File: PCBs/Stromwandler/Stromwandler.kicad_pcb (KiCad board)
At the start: 2 copper layers, 30 x 30 mm, 10 parts, among them J1 Conn_02x05_Odd_Even, J4 2X, U1 HO15-NPxSP33

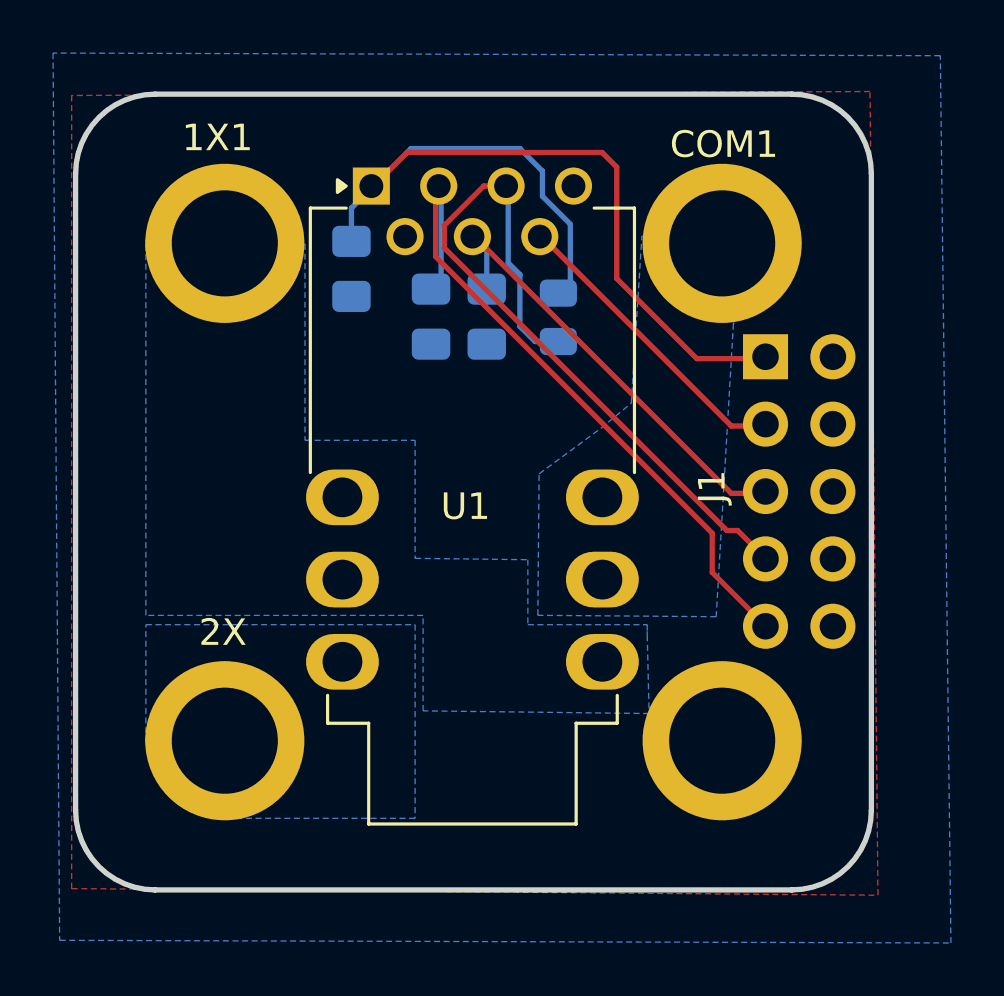
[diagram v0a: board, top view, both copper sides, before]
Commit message: Korrekturen: Anordnung 4mm-Pins Tausch Stecker Pin 5 7 (Uref, OCD) GND Vias (noch mehr  notwendig / Anordnung pruefen)
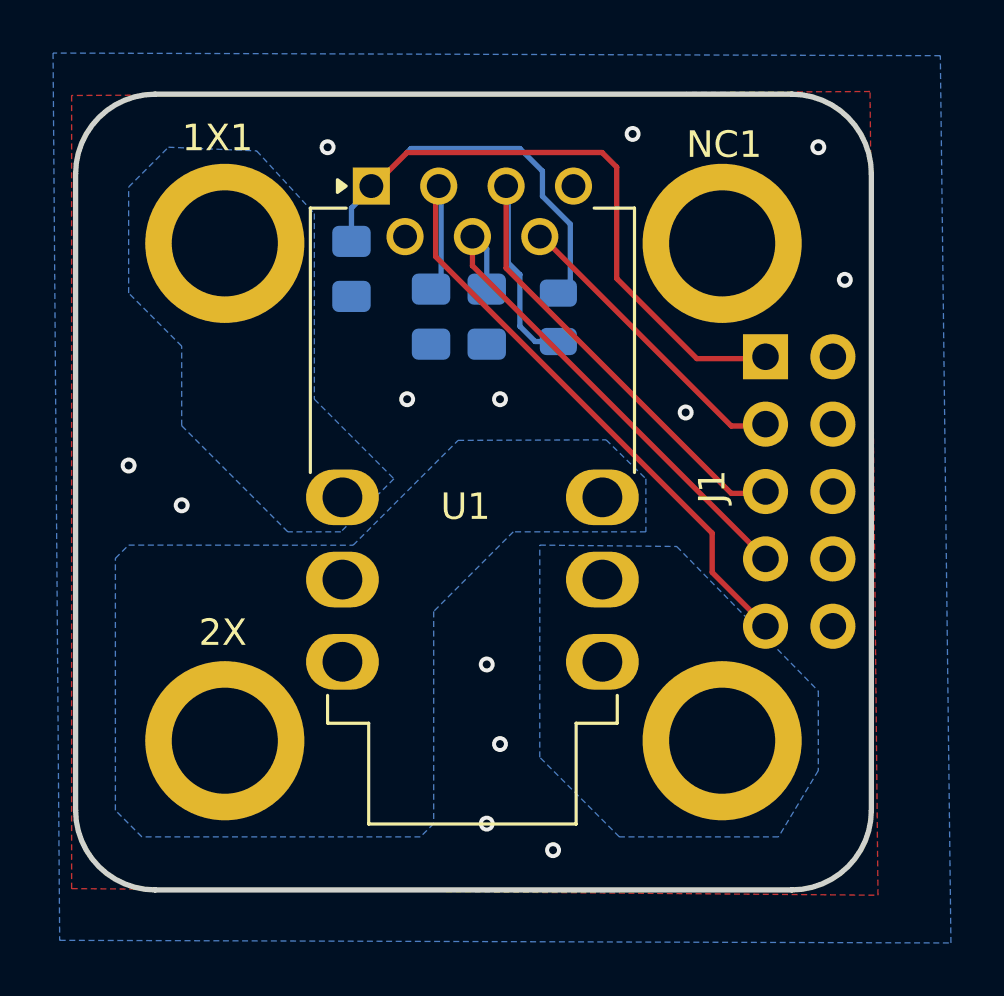
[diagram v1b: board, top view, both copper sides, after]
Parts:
- J4: value 2X -> IN
- renumbered COM1 to NC1
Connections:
- net Net-(J1-Pin_10) renamed GND
- C1 pad 2: Net-(J1-Pin_5) -> Net-(J1-Pin_7)
- J4 pad 1: unconnected-(J4-Pin_1-Pad1) -> Net-(J4-Pin_1)
- NC1 pad 1: Net-(COM1-Pin_1) -> unconnected-(NC1-Pin_1-Pad1)
- R1 pad 1: Net-(J1-Pin_7) -> Net-(J1-Pin_5)
- U1 pad 10: Net-(1X1-Pin_1) -> Net-(J4-Pin_1)
- U1 pad 12: Net-(1X1-Pin_1) -> Net-(3X1-Pin_1)
- U1 pad 4: Net-(J1-Pin_5) -> Net-(J1-Pin_7)
- U1 pad 5: Net-(J1-Pin_7) -> Net-(J1-Pin_5)
- U1 pad 8: Net-(COM1-Pin_1) -> Net-(3X1-Pin_1)
- U1 pad 9: Net-(COM1-Pin_1) -> Net-(J4-Pin_1)
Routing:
- net Net-(J1-Pin_7): track 28.1 -> 19.5 mm
- net Net-(J1-Pin_5): track 17.8 -> 23.6 mm
- net unconnected-(J4-Pin_1-Pad1): track 1.07 -> 0.00 mm
- net Net-(J4-Pin_1): track 0.00 -> 1.07 mm
- net GND: vias 0 -> 13
- added copper zone on B.Cu, net Net-(J4-Pin_1)
- removed copper zone on B.Cu, net Net-(COM1-Pin_1)

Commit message: Vias und R
Neue platzierung von Vias und R.
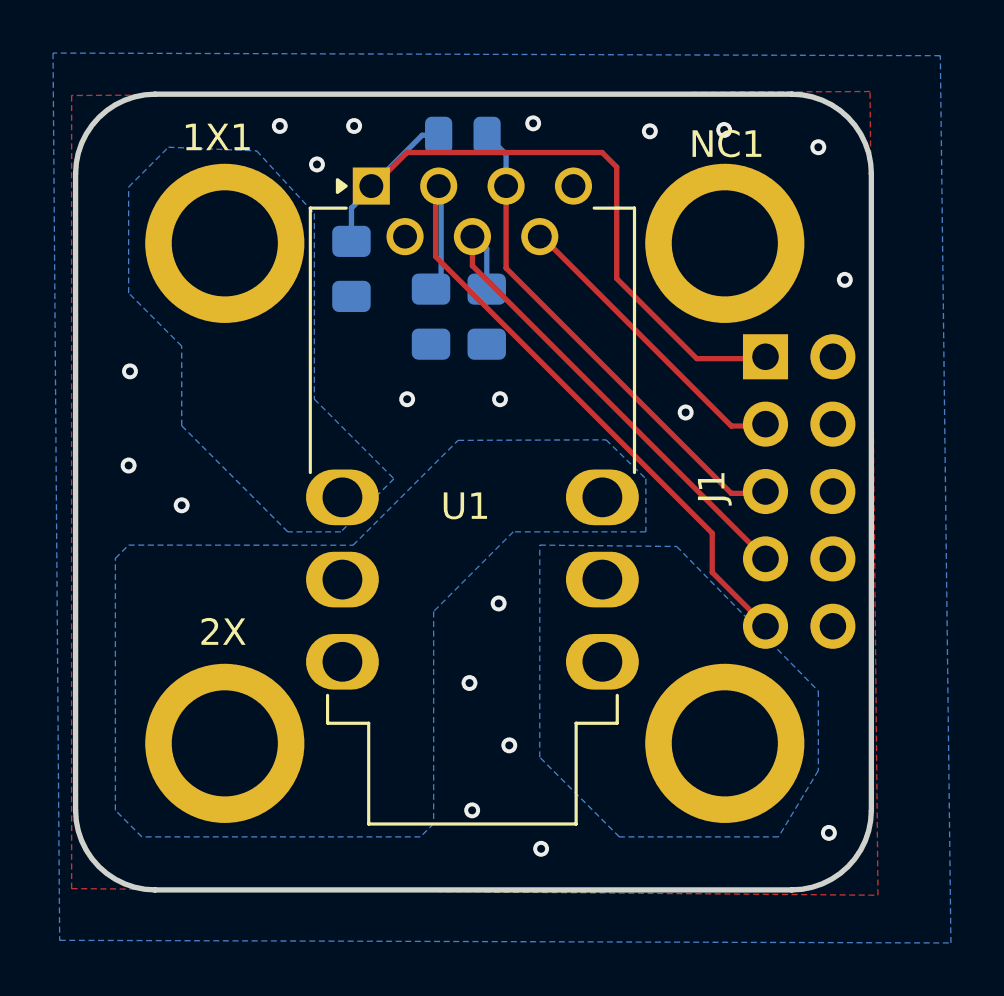
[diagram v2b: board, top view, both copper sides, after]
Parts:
- moved R1 7.75 mm to (99.6, 86.5), turned to 180 degrees
- moved J4 0.14 mm to (109.5, 109.5)
- moved 3X1 0.10 mm to (90.6, 109.5)
- moved NC1 0.10 mm to (109.5, 90.6)
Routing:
- net Net-(J1-Pin_1): track 36.0 -> 26.8 mm
- net Net-(J1-Pin_5): track 23.6 -> 18.7 mm
- net GND: vias 13 -> 20
